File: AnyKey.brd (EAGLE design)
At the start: 92 x 70 mm, 101 parts, among them SW1 EVQQ, SW10 EVQQ, SW2 EVQQ, SW3 EVQQ, SW4 EVQQ, SW5 EVQQ, SW6 EVQQ, SW7 EVQQ, SW8 EVQQ, SW9 EVQQ, U3 AP2112K-3.3V

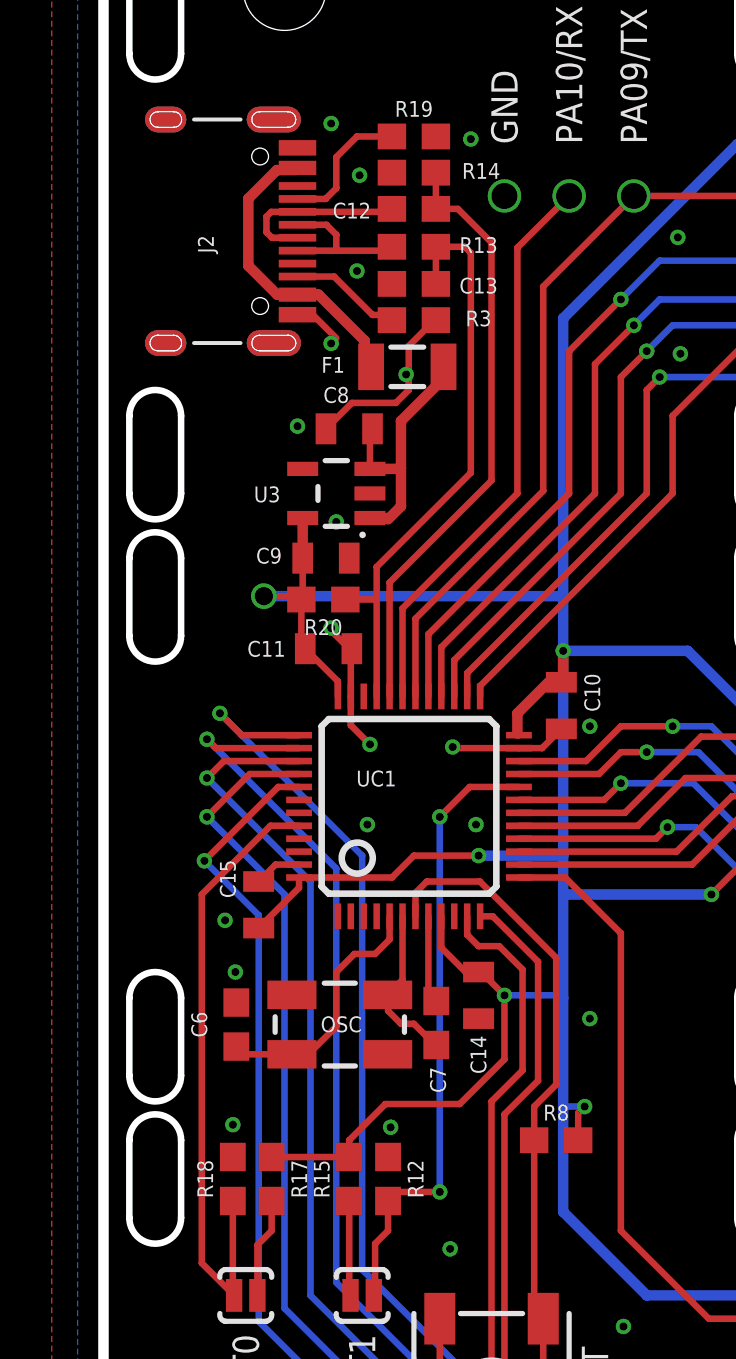
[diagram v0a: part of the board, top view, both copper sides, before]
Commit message: Initial cleanup, correctted some misplaced names in top silkscreen
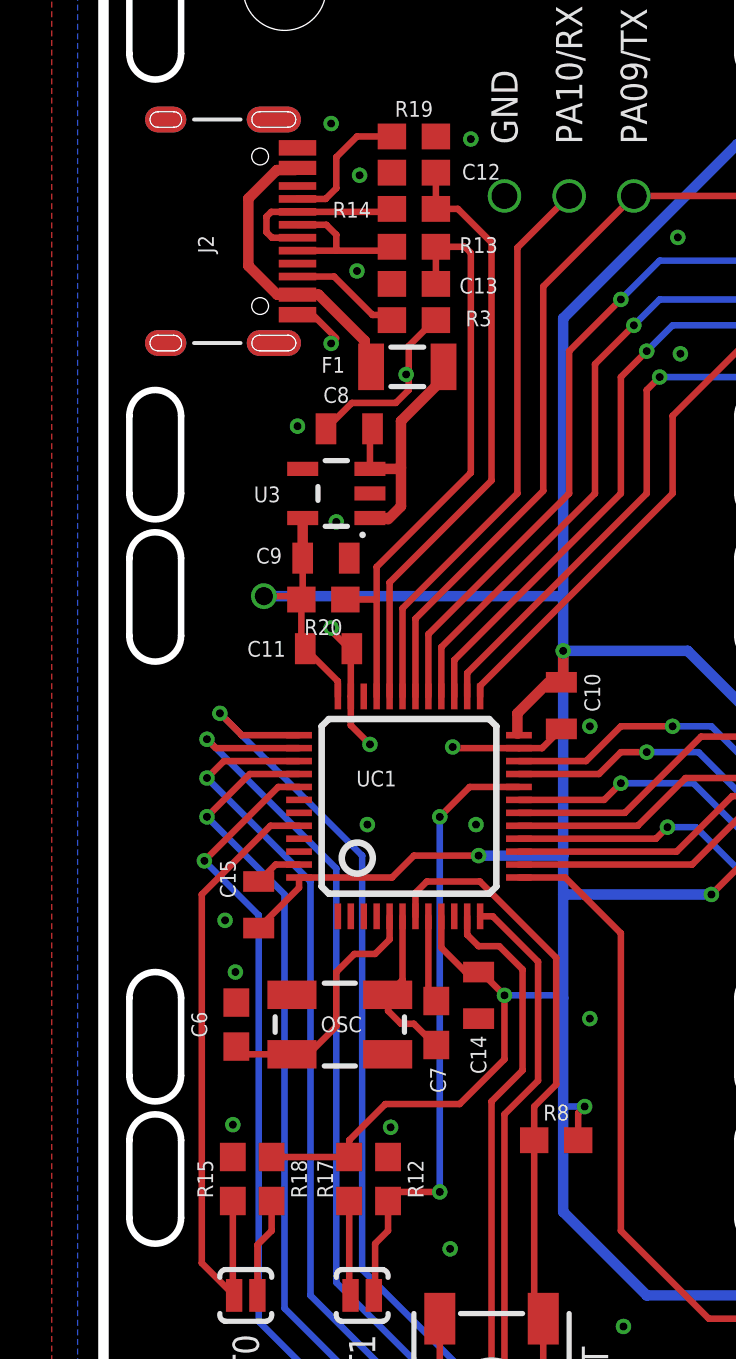
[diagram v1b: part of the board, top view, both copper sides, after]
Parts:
- C1, C10, C11, C14, C15, C18, C19, C2, C20, C23, C24, C25, C28, C29, C3, C30, C33, C34, C35, C38, C39, C40, C43, C44, C45, C48, C49, C50, C53, C54, C55, C8: device SparkFun-Capacitors:0805 -> AnyKey:0805
- C12, C13, C16, C21, C26, C31, C36, C41, C46, C5, C51: device SparkFun-Capacitors:0603 -> AnyKey:0603
- C17, C22, C27, C32, C37, C4, C42, C47, C52, C9: value 2.2uF -> 1.0uF; device SparkFun-Capacitors:0805 -> AnyKey:0805
- C6, C7: value 18pF -> 47pF; device SparkFun-Capacitors:0603 -> AnyKey:0603
- F1: device SparkFun-PowerIC:PTC-1206 -> AnyKey:PTC-1206
- J2: device SparkFun-Connectors:USB-C-16P -> AnyKey:USB-C-16P
- OLED1, OLED2, OLED3, OLED4, OLED5, OLED6, OLED7, OLED8, OLED9: device microView-temp:OLED-0.66-64X48 -> AnyKey:OLED-0.66-64X48
- OSC: device SparkFun2:CRYSTAL-SMD-5X3 -> AnyKey:CRYSTAL-SMD-5X3
- R1, R10, R11, R2, R4, R5, R6, R7, R9: value 390k -> 10k; device SparkFun-Resistors:0603 -> AnyKey:0603
- R12, R13, R14, R15, R8: device SparkFun-Resistors:0603 -> AnyKey:0603
- R16, R17, R18: value 1k -> 10k; device SparkFun-Resistors:0603 -> AnyKey:0603
- R19, R3: value 5.1k -> 10k; device SparkFun-Resistors:0603 -> AnyKey:0603
- R20: value 1k5 -> 10k; device SparkFun-Resistors:0603 -> AnyKey:0603
- SJ1, SJ2: value (none) -> JUMPER-PAD-2-NOYES_SILK; device SparkFun-Passives:PAD-JUMPER-2-NO_YES_SILK -> AnyKey:PAD-JUMPER-2-NO_YES_SILK
- SW1, SW10, SW2, SW3, SW4, SW5, SW6, SW7, SW8, SW9: device microbuilder:EVQ-Q2_SMALLER -> AnyKey:EVQ-Q2_SMALLER
- U3: device SparkFun-PowerIC:SOT23-5 -> AnyKey:SOT23-5
- UC1: device stm32:LQFP48 -> AnyKey:LQFP48
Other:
- board text added: "AnyKey v0.1 Chilluminaten 01/2021 github.com/The-AnyKey-Project"
- board text removed: "Keybon REV 1.1 Maximilian Kern 12/2020 github.com/CoretechR"

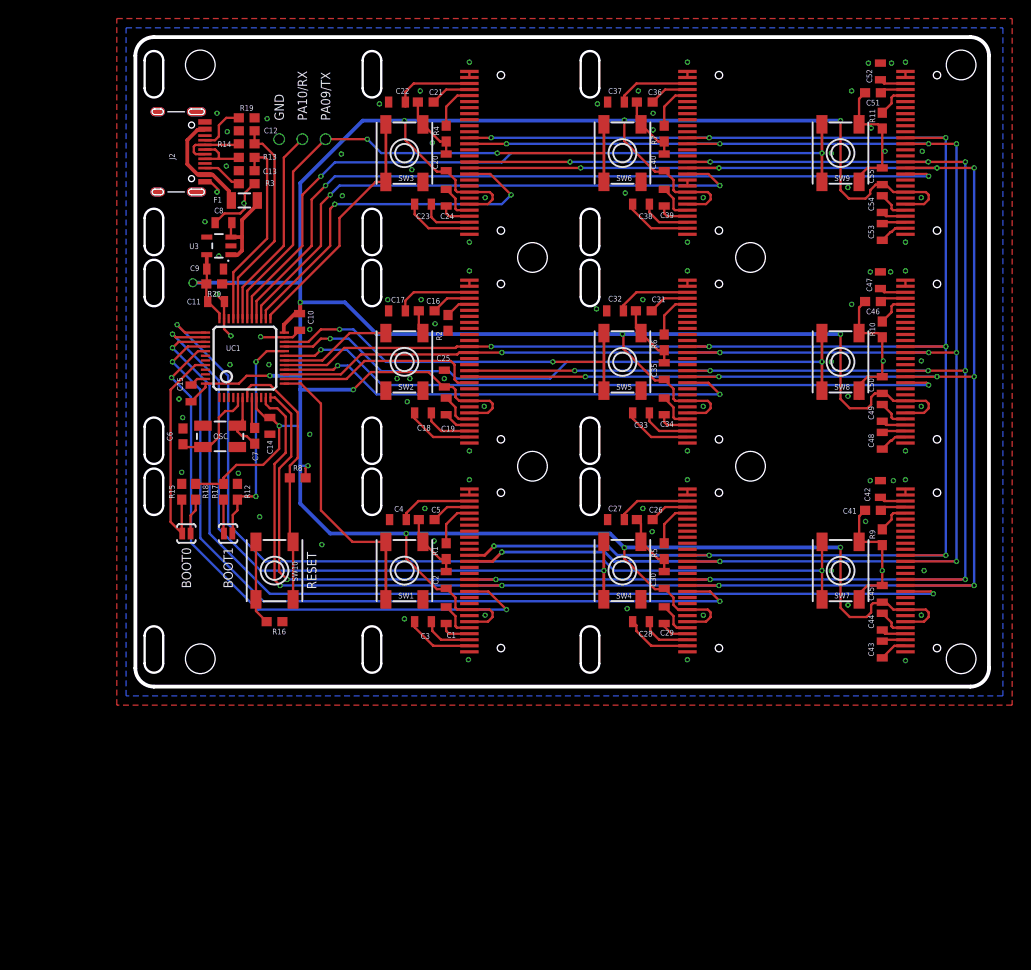
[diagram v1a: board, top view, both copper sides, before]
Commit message: Implemented Auto-Reset, Added WS2812 (WORK IN PROGRESS)
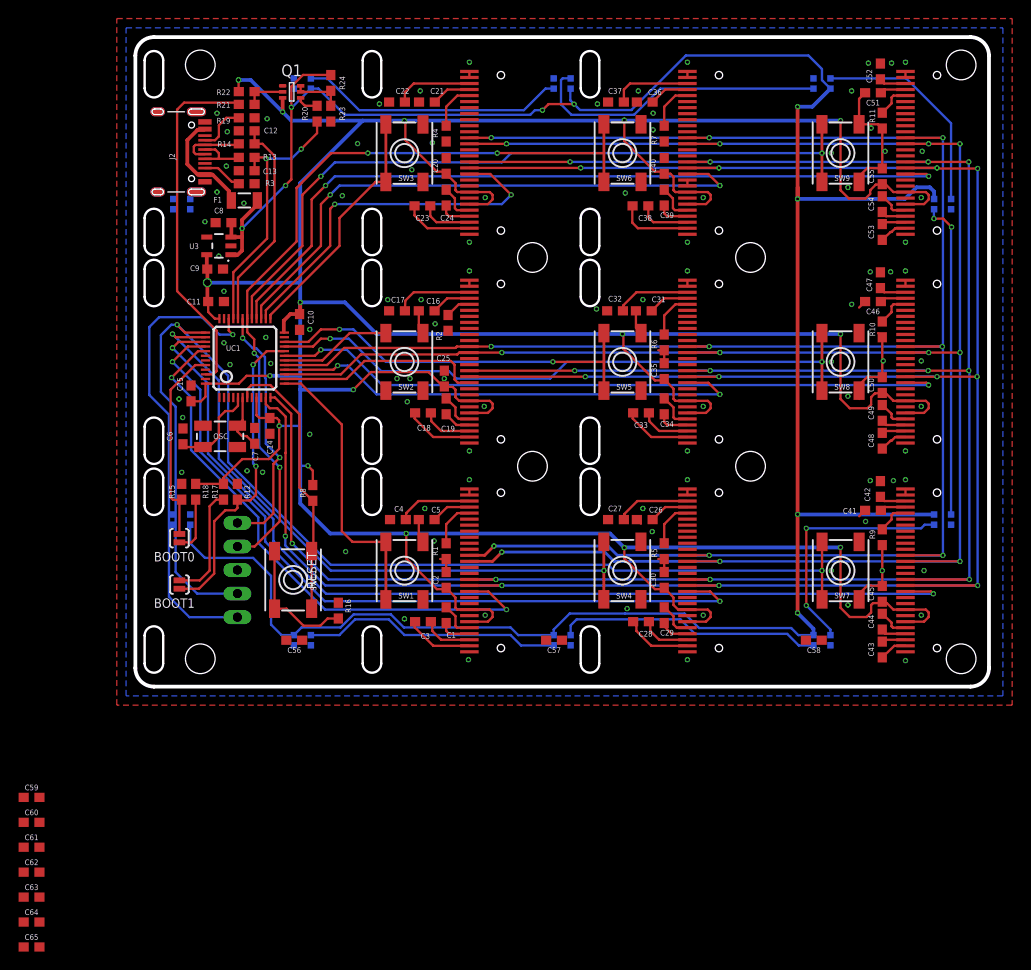
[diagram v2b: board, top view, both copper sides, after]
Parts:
- added C56, C57, C58, C59, C60, C61, C62, C63, C64, C65: 1uF, AnyKey:0603
- added D1, D10, D2, D3, D4, D5, D6, D7, D8, D9: WS2812_2020, AnyKey:WS2812_2020
- added JP1: DEBUG, AnyKey:1X05/90
- added Q1: BC847S, AnyKey:SOT-363
- added R21: 1k, AnyKey:0603
- added R22: 47k, AnyKey:0603
- added R23: 36k, AnyKey:0603
- added R24: 10k, AnyKey:0603
- C1, C10, C11, C14, C15, C18, C19, C2, C20, C23, C24, C25, C28, C29, C3, C30, C33, C34, C35, C38, C39, C40, C43, C44, C45, C48, C49, C50, C53, C54, C55, C8: device AnyKey:0805 -> AnyKey:0603
- C17, C22, C27, C32, C37, C4, C42, C47, C52, C9: value 1.0uF -> 2.2uF; device AnyKey:0805 -> AnyKey:0603
- C6, C7: value 47pF -> 18pF
- J2: value (none) -> SOFNG MC-311D
- R1, R10, R11, R2, R4, R5, R6, R7, R9: value 10k -> 390k
- R16, R17, R18: value 10k -> 1k
- R19, R3: value 10k -> 5k1
- R20: value 10k -> 1k5
- SW1, SW10, SW2, SW3, SW4, SW5, SW6, SW7, SW8, SW9: value EVQQ -> B3FS-1000P
- moved R20 21.4 mm to (19.6, 61.8), turned to 90 degrees
- moved SJ1 7.60 mm to (4.75, 11.0), turned to 90 degrees
- moved R16 6.98 mm to (21.9, 8.19), turned to 270 degrees
- moved R8 2.30 mm to (19.1, 20.9), turned to 90 degrees
- moved SW10 2.24 mm to (17.0, 11.5)
- moved SJ2 0.90 mm to (4.75, 16.0), turned to 270 degrees
- moved C20 0.38 mm to (33.5, 56.1)
- moved C40 0.38 mm to (57.0, 56.1)
- moved C23 0.20 mm to (30.9, 51.8)
- moved C38 0.20 mm to (54.4, 51.8)
- moved C21 0.12 mm to (31.4, 63.0)
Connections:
- removed net SW06: SW6.A, SW6.A', UC1.30
- removed net SW07: SW7.A, SW7.A', UC1.37
- new net DISC: R21.1, UC1.46
- new net N$15: Q1.P4, R20.2
- new net N$16: Q1.P5, Q1.P6, R23.2, R24.1
- new net N$17: Q1.P2, R21.2, R22.1
- new net N$18: D1.1, D2.3
- new net N$21: D2.1, D3.3
- new net N$22: D3.1, D4.3
- new net N$23: D4.1, D5.3
- new net N$24: D5.1, D6.3
- new net N$25: D6.1, D7.3
- new net N$26: D7.1, D8.3
- new net N$27: D8.1, D9.3
- new net N$28: D10.3, D9.1
- new net SW06/UART1_TX: JP1.2, SW6.A, SW6.A', UC1.30
- new net SW07/SWCLK: JP1.4, SW7.A, SW7.A', UC1.37
- new net SWDIO: JP1.5, UC1.34
- new net WS2812: D1.3, UC1.45
- net 3.3V: now also Q1.P3, R22.2; no longer R20.2
- net GND: now also C56.2, C57.2, C58.2, C59.2, C60.2, C61.2, C62.2, C63.2, C64.2, C65.2, D1.2, D10.2, D2.2, D3.2, D4.2, D5.2, D6.2, D7.2, D8.2, D9.2, JP1.3, Q1.P1, R23.1
- net SW02: now also SW2.A'
- net UART1_RX: now also JP1.1
- net V_USB: now also C56.1, C57.1, C58.1, C59.1, C60.1, C61.1, C62.1, C63.1, C64.1, C65.1, D1.4, D10.4, D2.4, D3.4, D4.4, D5.4, D6.4, D7.4, D8.4, D9.4, R24.2
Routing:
- net V_USB: track 10.3 -> 274.4 mm, vias 0 -> 9
- net SW07/SWCLK: track 0.00 -> 131.6 mm, vias 0 -> 2
- net SW07: track 99.5 -> 0.00 mm, vias 2 -> 0
- net SW06/UART1_TX: track 0.00 -> 86.2 mm, vias 0 -> 4
- net SW06: track 59.7 -> 0.00 mm, vias 3 -> 0
- net GND: track 112.5 -> 54.7 mm, vias 97 -> 96
- net SWDIO: track 0.00 -> 50.3 mm, vias 0 -> 1
- net DISC: track 0.00 -> 38.3 mm
- net N$23: track 0.00 -> 34.4 mm, vias 0 -> 2
- net N$25: track 0.00 -> 32.6 mm
- net N$21: track 0.00 -> 28.7 mm
- net N$26: track 0.00 -> 28.6 mm
- net N$18: track 0.00 -> 28.0 mm
- net N$22: track 0.00 -> 26.5 mm, vias 0 -> 2
- net N$24: track 0.00 -> 23.2 mm
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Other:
- board text added: "PA13/SWDIO"
- board text added: "PA14/SWCLK"
